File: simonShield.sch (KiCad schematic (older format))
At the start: 7 parts, among them Q1 BC547, U1 BUZZER

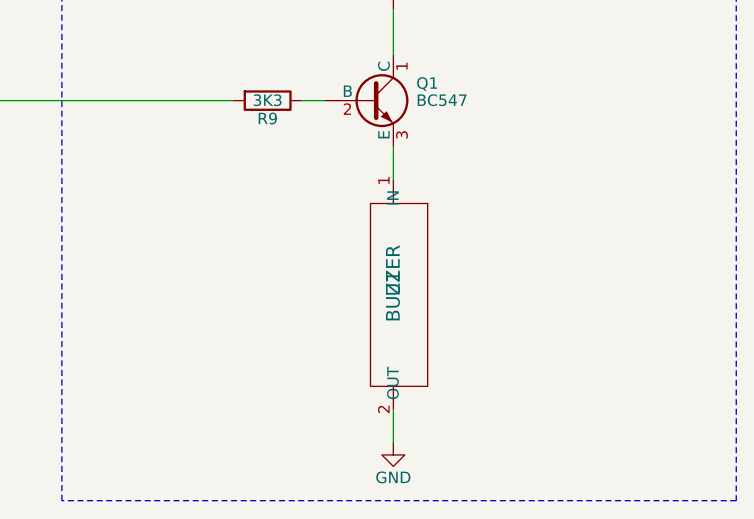
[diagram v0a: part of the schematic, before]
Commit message: Version 1 practicamente terminada de poncho Simon con EDU CIAA.
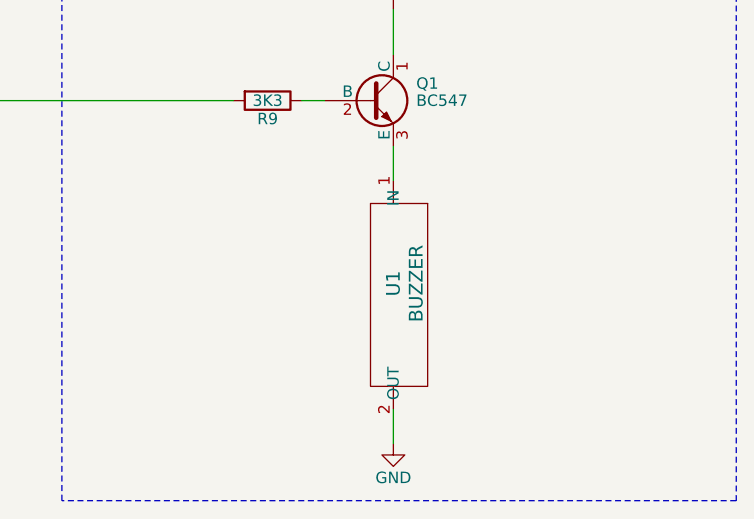
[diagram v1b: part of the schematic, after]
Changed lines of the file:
@@
 P 9500 5300
 F 0 "U1" H 9500 5300 60  0000 C CNN
-F 1 "BUZZER" H 9500 5300 60  0000 C CNN
+F 1 "BUZZER" H 9500 5400 60  0000 C CNN
 F 2 "simonShield:MagneticBuzzer_ProSignal_ABT-410-RC" H 9500 5300 60  0001 C CNN
 F 3 "" H 9500 5300 60  0000 C CNN

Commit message: Version luego de cambiar los pines y agregar dos resistencias de puentes.@
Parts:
- added R_THT_SMALL? (x2): R, symbol R
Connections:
- net GND: now also R_THT_SMALL?.1, R_THT_SMALL?.1, R_THT_SMALL?.2, R_THT_SMALL?.2
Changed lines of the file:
@@
 	1    0    0    -1
 $EndComp
+$Comp
+L R R_THT_SMALL?
+U 1 1 59572DE1
+P 2250 5400
+F 0 "R_THT_SMALL?" V 2330 5400 50  0000 C CNN
+F 1 "R" V 2250 5400 50  0000 C CNN
+F 2 "" V 2180 5400 50  0000 C CNN
+F 3 "" H 2250 5400 50  0000 C CNN
+	1    2250 5400
+	1    0    0    -1
+$EndComp
+$Comp
+L R R_THT_SMALL?
+U 1 1 59572EFC
+P 2700 5400
+F 0 "R_THT_SMALL?" V 2780 5400 50  0000 C CNN
+F 1 "R" V 2700 5400 50  0000 C CNN
+F 2 "" V 2630 5400 50  0000 C CNN
+F 3 "" H 2700 5400 50  0000 C CNN
+	1    2700 5400
+	1    0    0    -1
+$EndComp
+$Comp
+L GND #PWR?
+U 1 1 59573C63
+P 2700 5850
+F 0 "#PWR?" H 2700 5600 50  0001 C CNN
+F 1 "GND" H 2700 5700 50  0000 C CNN
+F 2 "" H 2700 5850 50  0000 C CNN
+F 3 "" H 2700 5850 50  0000 C CNN
+	1    2700 5850
+	1    0    0    -1
+$EndComp
+Wire Wire Line
+	2700 5550 2700 5850
+Wire Wire Line
+	2700 5250 2700 5000
+Wire Wire Line
+	2700 5000 2950 5000
+Wire Wire Line
+	2950 5000 2950 5750
+Wire Wire Line
+	2950 5750 2700 5750
+Connection ~ 2700 5750
+$Comp
+L GND #PWR?
+U 1 1 59573F0D
+P 2250 5850
+F 0 "#PWR?" H 2250 5600 50  0001 C CNN
+F 1 "GND" H 2250 5700 50  0000 C CNN
+F 2 "" H 2250 5850 50  0000 C CNN
+F 3 "" H 2250 5850 50  0000 C CNN
+	1    2250 5850
+	1    0    0    -1
+$EndComp
+Wire Wire Line
+	2250 5550 2250 5850
+Wire Wire Line
+	2250 5250 2250 5000
+Wire Wire Line
+	2250 5000 2000 5000
+Wire Wire Line
+	2000 5000 2000 5750
+Wire Wire Line
+	2000 5750 2250 5750
+Connection ~ 2250 5750
 $EndSCHEMATC

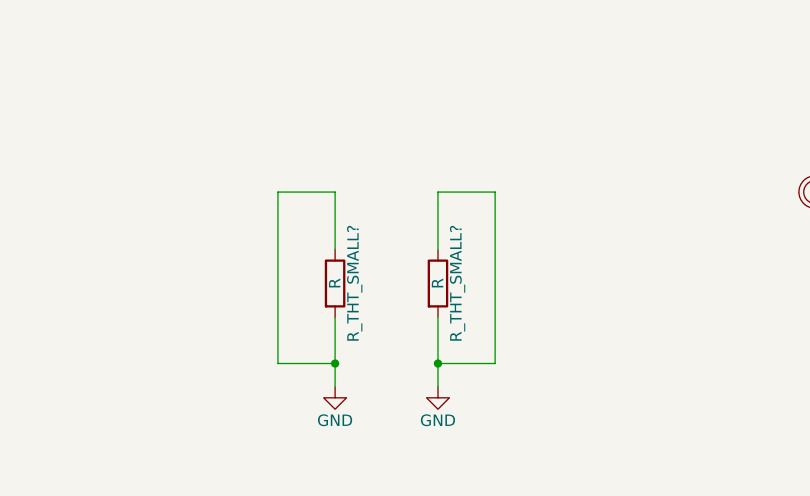
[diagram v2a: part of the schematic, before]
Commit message: Version totalmente ruteada. Previo a hacer puentes con resistencia y a serigrafia.
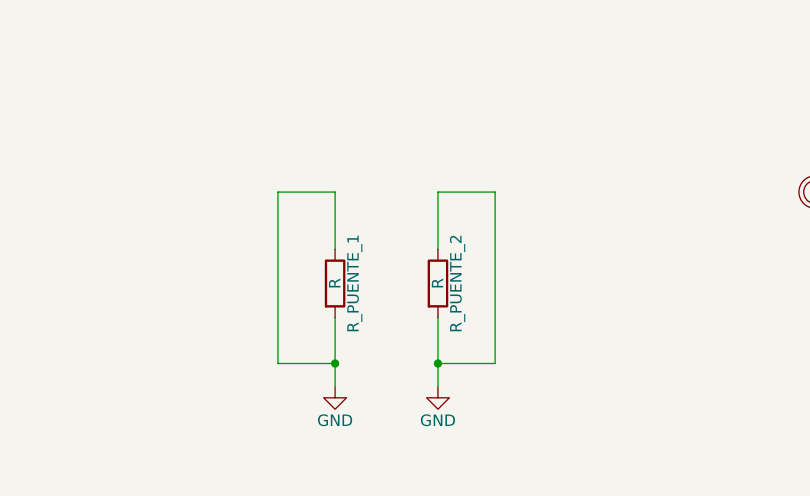
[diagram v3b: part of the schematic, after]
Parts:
- R_PUENTE_1, R_PUENTE_2: renamed from R_THT_SMALL?; footprint (none) -> Resistors_THT:R_Axial_DIN0207_L6.3mm_D2.5mm_P10.16mm_Horizontal
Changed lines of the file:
@@
 $EndComp
 $Comp
-L R R_THT_SMALL?
+L R R_PUENTE_1
 U 1 1 59572DE1
 P 2250 5400
-F 0 "R_THT_SMALL?" V 2330 5400 50  0000 C CNN
+F 0 "R_PUENTE_1" V 2330 5400 50  0000 C CNN
 F 1 "R" V 2250 5400 50  0000 C CNN
-F 2 "" V 2180 5400 50  0000 C CNN
+F 2 "Resistors_THT:R_Axial_DIN0207_L6.3mm_D2.5mm_P10.16mm_Horizontal" V 2180 5400 50  0001 C CNN
 F 3 "" H 2250 5400 50  0000 C CNN
 	1    2250 5400
@@
 $EndComp
 $Comp
-L R R_THT_SMALL?
+L R R_PUENTE_2
 U 1 1 59572EFC
 P 2700 5400
-F 0 "R_THT_SMALL?" V 2780 5400 50  0000 C CNN
+F 0 "R_PUENTE_2" V 2780 5400 50  0000 C CNN
 F 1 "R" V 2700 5400 50  0000 C CNN
-F 2 "" V 2630 5400 50  0000 C CNN
+F 2 "Resistors_THT:R_Axial_DIN0207_L6.3mm_D2.5mm_P10.16mm_Horizontal" V 2630 5400 50  0001 C CNN
 F 3 "" H 2700 5400 50  0000 C CNN
 	1    2700 5400
@@
 $EndComp
 $Comp
-L GND #PWR?
+L GND #PWR03
 U 1 1 59573C63
 P 2700 5850
-F 0 "#PWR?" H 2700 5600 50  0001 C CNN
+F 0 "#PWR03" H 2700 5600 50  0001 C CNN
 F 1 "GND" H 2700 5700 50  0000 C CNN
 F 2 "" H 2700 5850 50  0000 C CNN
@@
 Connection ~ 2700 5750
 $Comp
-L GND #PWR?
+L GND #PWR04
 U 1 1 59573F0D
 P 2250 5850
-F 0 "#PWR?" H 2250 5600 50  0001 C CNN
+F 0 "#PWR04" H 2250 5600 50  0001 C CNN
 F 1 "GND" H 2250 5700 50  0000 C CNN
 F 2 "" H 2250 5850 50  0000 C CNN
